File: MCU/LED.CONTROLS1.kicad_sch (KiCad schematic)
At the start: 21 parts, among them U3 HHG1D-1, U4 AMC3302QDWERQ1

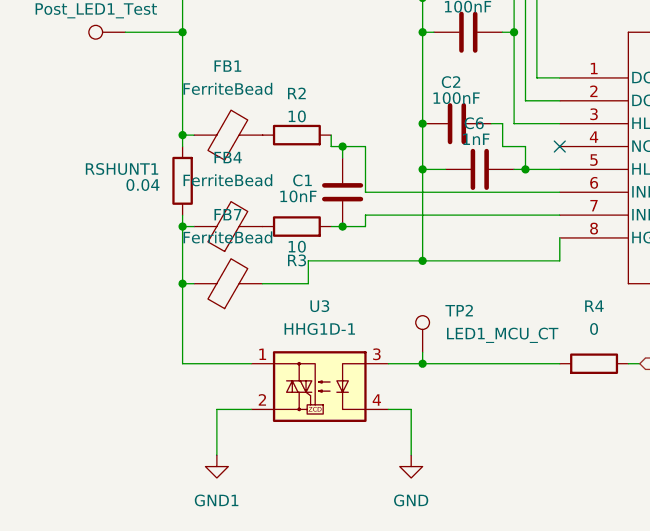
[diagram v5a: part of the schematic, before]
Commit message: almost done with MCU: need to change TP names, adjust RTD on MCU
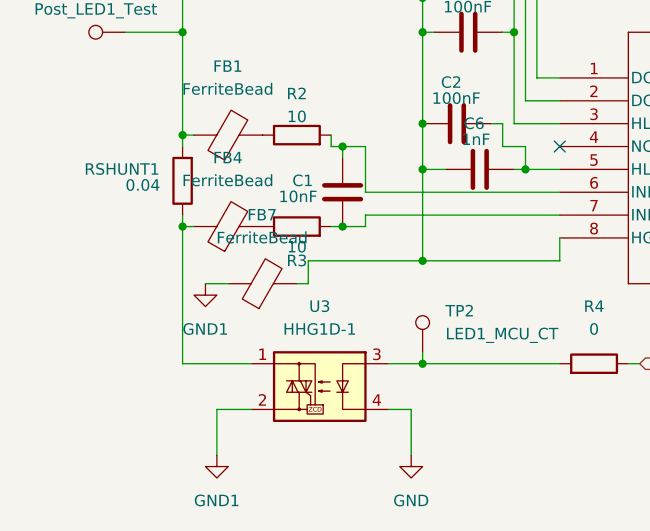
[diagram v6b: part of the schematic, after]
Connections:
- net GND1: now also FB7.1
- net at FB4.1, RSHUNT1.1, U3.1: no longer FB7.1
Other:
- moved on the sheet: FB7
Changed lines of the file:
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@@
-	)
-	(junction
-		(at 88.9 109.22)
-		(diameter 0)
-		(color 0 0 0 0)
 	)
 	(junction
@@
 	(wire
 		(pts
-			(xy 88.9 102.87) (xy 88.9 109.22)
+			(xy 88.9 102.87) (xy 88.9 118.11)
 		)
 		(stroke
@@
 	(wire
 		(pts
-			(xy 102.87 109.22) (xy 97.79 109.22)
+			(xy 102.87 109.22) (xy 101.6 109.22)
 		)
 		(stroke
@@
 	(wire
 		(pts
-			(xy 90.17 109.22) (xy 88.9 109.22)
+			(xy 91.44 109.22) (xy 93.98 109.22)
 		)
 		(stroke
@@
 		(pts
 			(xy 123.19 91.44) (xy 124.46 91.44)
-		)
-		(stroke
-			(width 0)
-			(type default)
-		)
-	)
-	(wire
-		(pts
-			(xy 88.9 109.22) (xy 88.9 118.11)
 		)
 		(stroke
@@
 	)
 	(symbol
+		(lib_id "power:GND1")
+		(at 91.44 109.22 0)
+		(unit 1)
+		(exclude_from_sim no)
+		(in_bom yes)
+		(on_board yes)
+		(dnp no)
+		(fields_autoplaced yes)
+		(property "Reference" "#PWR05"
+			(at 91.44 115.57 0)
+			(effects
+				(font
+					(size 1.27 1.27)
+				)
+				(hide yes)
+			)
+		)
+		(property "Value" "GND1"
+			(at 91.44 114.3 0)
+			(effects
+				(font
+					(size 1.27 1.27)
+				)
+			)
+		)
+		(property "Footprint" ""
+			(at 91.44 109.22 0)
+			(effects
+				(font
+					(size 1.27 1.27)
+				)
+				(hide yes)
+			)
+		)
+		(property "Datasheet" ""
+			(at 91.44 109.22 0)
+			(effects
+				(font
+					(size 1.27 1.27)
+				)
+				(hide yes)
+			)
+		)
+		(property "Description" "Power symbol creates a global label with name \"GND1\" , ground"
+			(at 91.44 109.22 0)
+			(effects
+				(font
+					(size 1.27 1.27)
+				)
+				(hide yes)
+			)
+		)
+		(pin "1"
+		)
+		(instances
+			(project "MCU"
+				(path "/56b3f3ef-07ec-480e-b5f8-5a7fd51b01f6/791b08aa-831e-4b43-99fd-f084e643ad78"
+					(reference "#PWR019")
+					(unit 1)
+				)
+				(path "/56b3f3ef-07ec-480e-b5f8-5a7fd51b01f6/c99b0c29-f7d0-435d-b42f-ec10dff428f4"
+					(reference "#PWR020")
+					(unit 1)
+				)
+				(path "/56b3f3ef-07ec-480e-b5f8-5a7fd51b01f6/ebe2158f-a1b2-4452-963c-f041e3feae05"
+					(reference "#PWR05")
+					(unit 1)
+				)
+			)
+		)
+	)
+	(symbol
 		(lib_id "Device:C")
 		(at 205.74 100.33 0)
@@
 	(symbol
 		(lib_id "Device:FerriteBead")
-		(at 93.98 109.22 90)
+		(at 97.79 109.22 90)
 		(unit 1)
 		(exclude_from_sim no)
@@
 		(fields_autoplaced yes)
 		(property "Reference" "FB7"
-			(at 93.9292 101.6 90)
+			(at 97.7392 101.6 90)
 			(effects
 				(font
@@
 		)
 		(property "Value" "FerriteBead"
-			(at 93.9292 104.14 90)
+			(at 97.7392 104.14 90)
 			(effects
 				(font
@@
 		)
 		(property "Footprint" "Resistor_SMD:R_0402_1005Metric_Pad0.72x0.64mm_HandSolder"
-			(at 93.98 110.998 90)
+			(at 97.79 110.998 90)
 			(effects
 				(font
@@
 		)
 		(property "Datasheet" "https://www.mouser.com/catalog/specsheets/Bourns_6-22-2022_MH1005_datasheet.pdf"
-			(at 93.98 109.22 0)
+			(at 97.79 109.22 0)
 			(effects
 				(font
@@
 		)
 		(property "Description" "Ferrite bead"
-			(at 93.98 109.22 0)
-			(effects
-				(font
+			(at 97.79 109.22 0)
+			(effects
+				(font

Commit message: final?
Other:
- note removed: "change D8 to a more conveniently located digital pin"
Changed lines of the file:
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@@
 	(generator_version "9.0")
 	(paper "A4")
-	(text "change D8 to a more conveniently located digital pin"
-		(exclude_from_sim no)
-		(at 195.326 124.46 0)
-		(effects
-			(font
-				(size 1.27 1.27)
-			)
-		)
-	)
 	(junction
 		(at 88.9 92.71)

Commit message: final changes
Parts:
- C2, C3, C4, C5, C6, C7, C8, C9: footprint Capacitor_SMD:C_0201_0603Metric_Pad0.64x0.40mm_HandSolder -> Capacitor_SMD:C_0603_1608Metric_Pad1.08x0.95mm_HandSolder
- FB1, FB4, FB7: footprint Resistor_SMD:R_0402_1005Metric_Pad0.72x0.64mm_HandSolder -> Resistor_SMD:R_0603_1608Metric_Pad0.98x0.95mm_HandSolder
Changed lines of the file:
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@@
 			)
 		)
-		(property "Footprint" "Resistor_SMD:R_0402_1005Metric_Pad0.72x0.64mm_HandSolder"
+		(property "Footprint" "Resistor_SMD:R_0603_1608Metric_Pad0.98x0.95mm_HandSolder"
 			(at 93.98 94.488 90)
 			(effects
@@
 			)
 		)
-		(property "Datasheet" "https://www.mouser.com/catalog/specsheets/Bourns_6-22-2022_MH1005_datasheet.pdf"
+		(property "Datasheet" "https://www.bourns.com/docs/product-datasheets/MH1608.pdf"
 			(at 93.98 92.71 0)
 			(effects
@@
 			)
 		)
-		(property "Footprint" "Capacitor_SMD:C_0201_0603Metric_Pad0.64x0.40mm_HandSolder"
+		(property "Footprint" "Capacitor_SMD:C_0603_1608Metric_Pad1.08x0.95mm_HandSolder"
 			(at 206.7052 104.14 0)
 			(effects
@@
 			)
 		)
-		(property "Footprint" "Capacitor_SMD:C_0201_0603Metric_Pad0.64x0.40mm_HandSolder"
+		(property "Footprint" "Capacitor_SMD:C_0603_1608Metric_Pad1.08x0.95mm_HandSolder"
 			(at 116.84 65.7352 0)
 			(effects
@@
 			)
 		)
-		(property "Footprint" "Resistor_SMD:R_0402_1005Metric_Pad0.72x0.64mm_HandSolder"
+		(property "Footprint" "Resistor_SMD:R_0603_1608Metric_Pad0.98x0.95mm_HandSolder"
 			(at 97.79 110.998 90)
 			(effects
@@
 			)
 		)
-		(property "Datasheet" "https://www.mouser.com/catalog/specsheets/Bourns_6-22-2022_MH1005_datasheet.pdf"
+		(property "Datasheet" "https://www.bourns.com/docs/product-datasheets/MH1608.pdf"
 			(at 97.79 109.22 0)
 			(effects
@@
 			)
 		)
-		(property "Footprint" "Resistor_SMD:R_0402_1005Metric_Pad0.72x0.64mm_HandSolder"
+		(property "Footprint" "Resistor_SMD:R_0603_1608Metric_Pad0.98x0.95mm_HandSolder"
 			(at 93.98 104.648 90)
 			(effects
@@
 			)
 		)
-		(property "Datasheet" "https://www.mouser.com/catalog/specsheets/Bourns_6-22-2022_MH1005_datasheet.pdf"
+		(property "Datasheet" "https://www.bourns.com/docs/product-datasheets/MH1608.pdf"
 			(at 93.98 102.87 0)
 			(effects
@@
 			)
 		)
-		(property "Footprint" "Capacitor_SMD:C_0201_0603Metric_Pad0.64x0.40mm_HandSolder"
+		(property "Footprint" "Capacitor_SMD:C_0603_1608Metric_Pad1.08x0.95mm_HandSolder"
 			(at 118.11 97.4852 0)
 			(effects
@@
 			)
 		)
-		(property "Footprint" "Capacitor_SMD:C_0201_0603Metric_Pad0.64x0.40mm_HandSolder"
+		(property "Footprint" "Capacitor_SMD:C_0603_1608Metric_Pad1.08x0.95mm_HandSolder"
 			(at 115.57 92.4052 0)
 			(effects
@@
 			)
 		)
-		(property "Footprint" "Capacitor_SMD:C_0201_0603Metric_Pad0.64x0.40mm_HandSolder"
+		(property "Footprint" "Capacitor_SMD:C_0603_1608Metric_Pad1.08x0.95mm_HandSolder"
 			(at 116.84 74.6252 0)
 			(effects
@@
 			)
 		)
-		(property "Footprint" "Capacitor_SMD:C_0201_0603Metric_Pad0.64x0.40mm_HandSolder"
+		(property "Footprint" "Capacitor_SMD:C_0603_1608Metric_Pad1.08x0.95mm_HandSolder"
 			(at 213.0552 86.36 0)
 			(effects
@@
 			)
 		)
-		(property "Datasheet" "https://search.murata.co.jp/Ceramy/image/img/A01X/G101/ENG/GRM033C71C104KE14-01.pdf"
+		(property "Datasheet" "https://www.mouser.com/datasheet/3/72/1/KEM_C1002_X7R_SMD.pdf"
 			(at 212.09 82.55 0)
 			(effects
@@
 			)
 		)
-		(property "Description" "0.1 µF ±10% 16V Ceramic Capacitor X7S 0201 (0603 Metric)"
+		(property "Description" "Multilayer Ceramic Capacitors MLCC - SMD/SMT 50V 0.1uF X7R 0603 10%"
 			(at 212.09 82.55 0)
 			(effects
@@
 			)
 		)
-		(property "Footprint" "Capacitor_SMD:C_0201_0603Metric_Pad0.64x0.40mm_HandSolder"
+		(property "Footprint" "Capacitor_SMD:C_0603_1608Metric_Pad1.08x0.95mm_HandSolder"
 			(at 200.3552 104.14 0)
 			(effects
@@
 			)
 		)
-		(property "Footprint" "Capacitor_SMD:C_0201_0603Metric_Pad0.64x0.40mm_HandSolder"
+		(property "Footprint" "Capacitor_SMD:C_0603_1608Metric_Pad1.08x0.95mm_HandSolder"
 			(at 116.84 82.2452 0)
 			(effects
